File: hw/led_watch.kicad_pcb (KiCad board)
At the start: 4 copper layers, 29.6 x 29.6 mm, 96 parts, among them U3 M0G3507QDGS32RQ1, Y2 TXC-7C

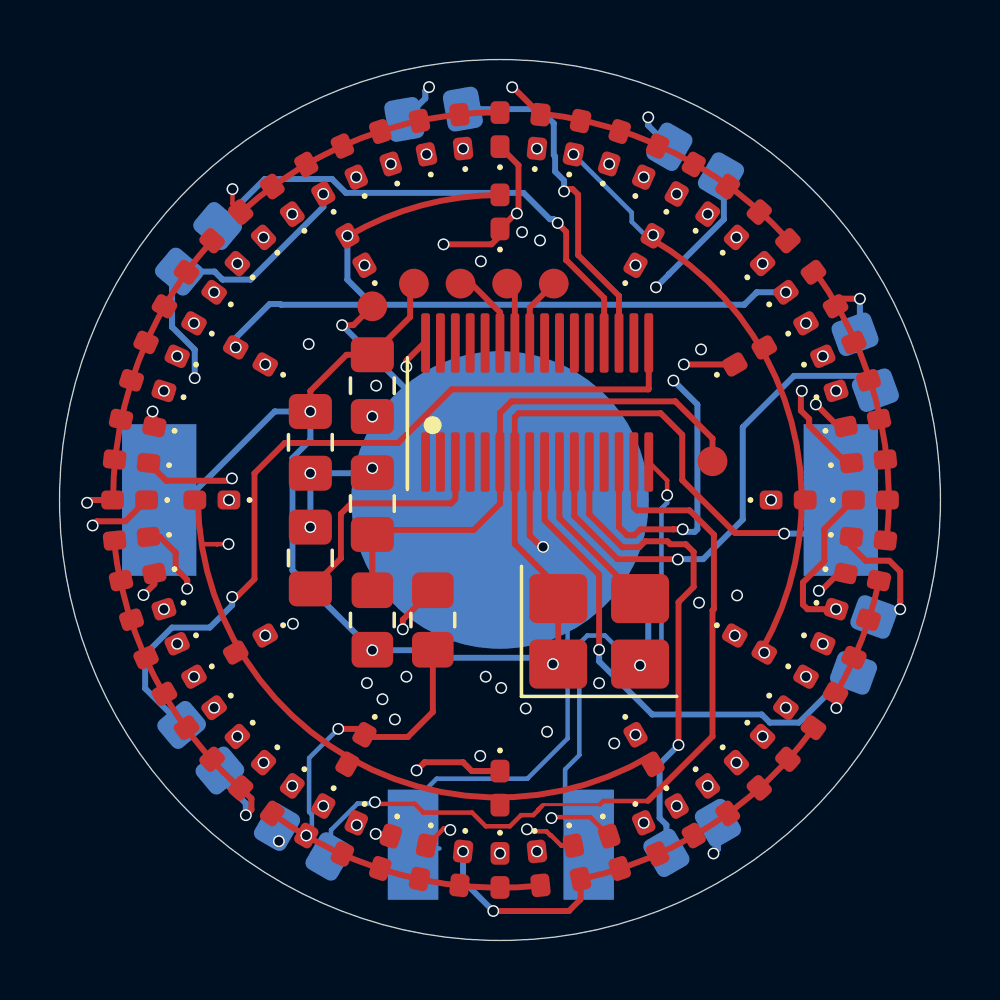
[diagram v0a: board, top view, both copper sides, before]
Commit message: cleanup hw dir, move readme
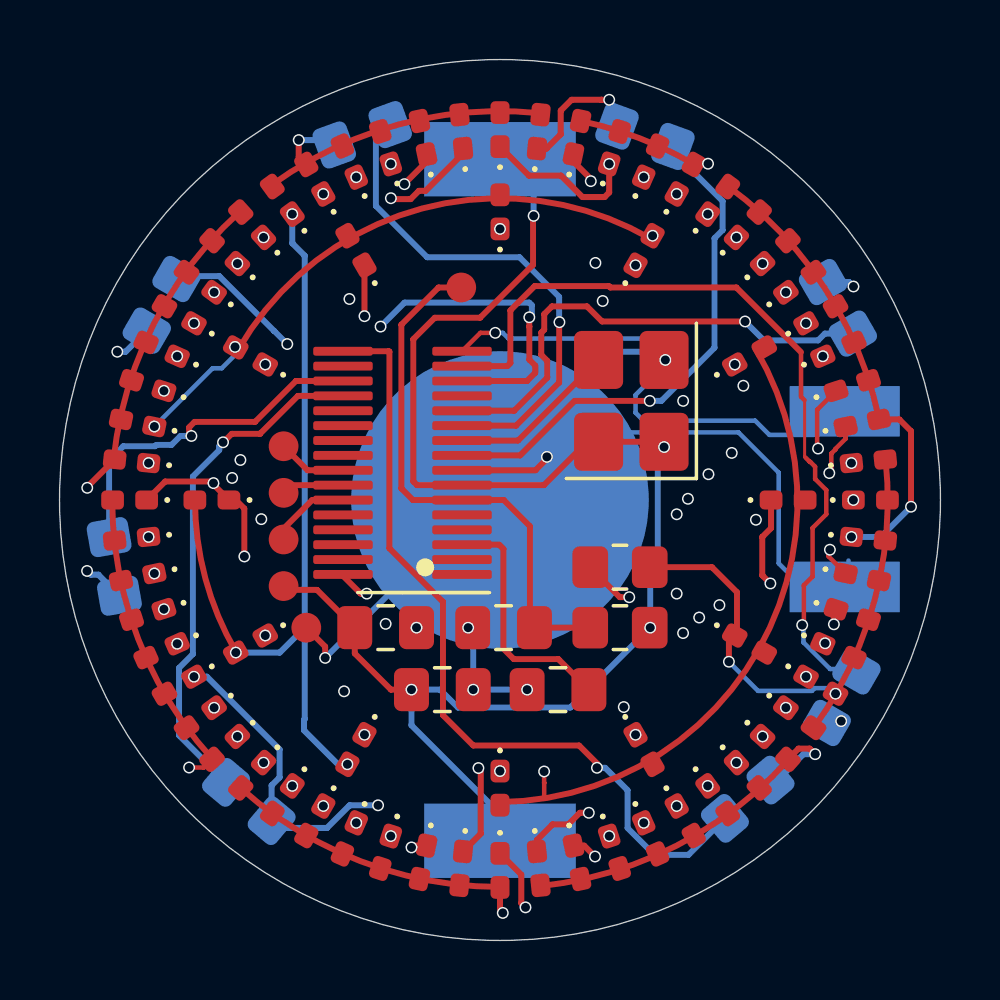
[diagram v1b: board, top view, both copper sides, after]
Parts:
- moved R7 18.7 mm to (118.6, 58.9), turned to -120 degrees
- moved R13 18.6 mm to (98.7, 62.4), turned to -40 degrees
- moved R3 18.6 mm to (112.0, 40.0), turned to 160 degrees
- moved R15 18.6 mm to (94.2, 54.5), turned to -80 degrees
- moved R17 18.6 mm to (95.8, 45.7), turned to -120 degrees
- moved R1 18.5 mm to (102.5, 40.0), turned to -160 degrees
- moved R5 18.5 mm to (118.5, 45.8), turned to 120 degrees
- moved R9 18.5 mm to (115.5, 62.3), turned to 40 degrees
- moved D1 17.6 mm to (108.5, 39.9), turned to 84 degrees
- moved D16 17.6 mm to (94.8, 50.9), turned to 174 degrees
- moved D18 17.6 mm to (94.8, 53.5), turned to -174 degrees
- moved D3 17.6 mm to (105.9, 39.9), turned to 96 degrees
- moved D31 17.6 mm to (105.9, 64.6), turned to -96 degrees
- moved D33 17.6 mm to (108.5, 64.6), turned to -84 degrees
- moved D46 17.6 mm to (119.5, 53.5), turned to -6 degrees
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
